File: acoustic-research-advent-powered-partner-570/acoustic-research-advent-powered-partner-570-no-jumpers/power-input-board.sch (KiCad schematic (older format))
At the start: 13 parts, among them J24 DNP, SW1 MAIN POWER

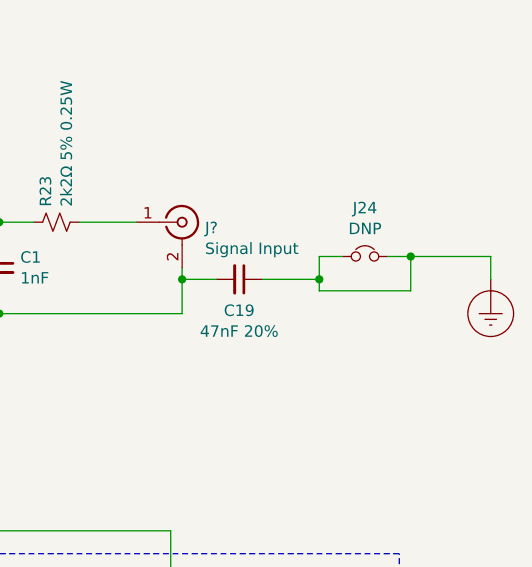
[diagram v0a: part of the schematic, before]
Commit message: simplified speghetti by using power rail symbols
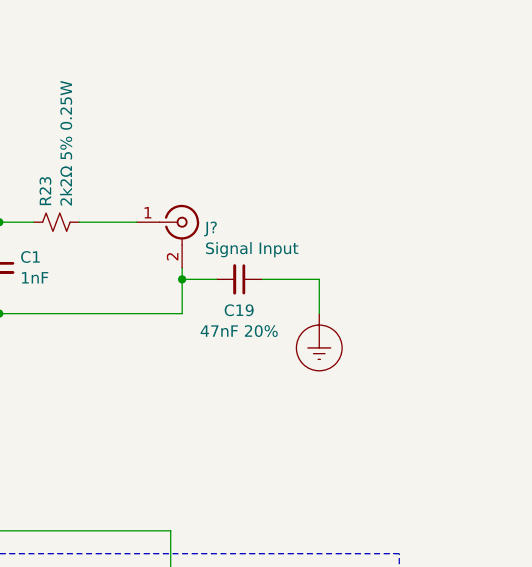
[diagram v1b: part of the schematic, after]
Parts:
- removed J24: DNP, symbol Device:Jumper_NC_Small
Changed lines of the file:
@@
-$EndComp
-$Comp
-L Device:Jumper_NC_Small J24
-U 1 1 6581408D
-P 6800 2500
-F 0 "J24" H 6800 2712 50  0000 C CNN
-F 1 "DNP" H 6800 2621 50  0000 C CNN
-F 2 "" H 6800 2500 50  0001 C CNN
-F 3 "~" H 6800 2500 50  0001 C CNN
-	1    6800 2500
-	1    0    0    -1
 $EndComp
 $Comp
 L power:Earth_Protective #PWR?
 U 1 1 65814E46
-P 7350 2600
-F 0 "#PWR?" H 7600 2350 50  0001 C CNN
-F 1 "Earth_Protective" H 7800 2450 50  0001 C CNN
-F 2 "" H 7350 2500 50  0001 C CNN
-F 3 "~" H 7350 2500 50  0001 C CNN
-	1    7350 2600
-	1    0    0    -1
-$EndComp
-Wire Wire Line
-	6900 2500 7000 2500
-Wire Wire Line
-	7350 2500 7350 2600
+P 6600 2750
+F 0 "#PWR?" H 6850 2500 50  0001 C CNN
+F 1 "Earth_Protective" H 7050 2600 50  0001 C CNN
+F 2 "" H 6600 2650 50  0001 C CNN
+F 3 "~" H 6600 2650 50  0001 C CNN
+	1    6600 2750
+	1    0    0    -1
+$EndComp
 $Comp
 L Connector_Generic:Conn_01x06 J?
@@
 Connection ~ 5200 2750
 Wire Wire Line
-	7000 2500 7000 2650
-Wire Wire Line
-	7000 2650 6600 2650
-Wire Wire Line
-	6600 2650 6600 2600
-Wire Wire Line
-	6600 2500 6700 2500
-Connection ~ 7000 2500
-Wire Wire Line
-	7000 2500 7350 2500
-Wire Wire Line
 	5550 2350 5800 2350
 Wire Wire Line
@@
 Wire Wire Line
 	6350 2600 6600 2600
-Connection ~ 6600 2600
-Wire Wire Line
-	6600 2600 6600 2500
 Wire Wire Line
 	3150 2750 5200 2750
@@
 Text Label 3750 2750 0    50   ~ 0
 AUDIO_GND
+Wire Wire Line
+	6600 2600 6600 2750
 $EndSCHEMATC
